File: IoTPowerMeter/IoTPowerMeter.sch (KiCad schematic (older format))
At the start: 50 parts, among them J1 Conn_01x01, J2 Conn_01x01, SW1 SW_SPDT, T1 VPP16-310, U1 UA78M33CDCYR, U2 ATM90E26-YU-B, U3 PHOTON, Y1 8.192MHz

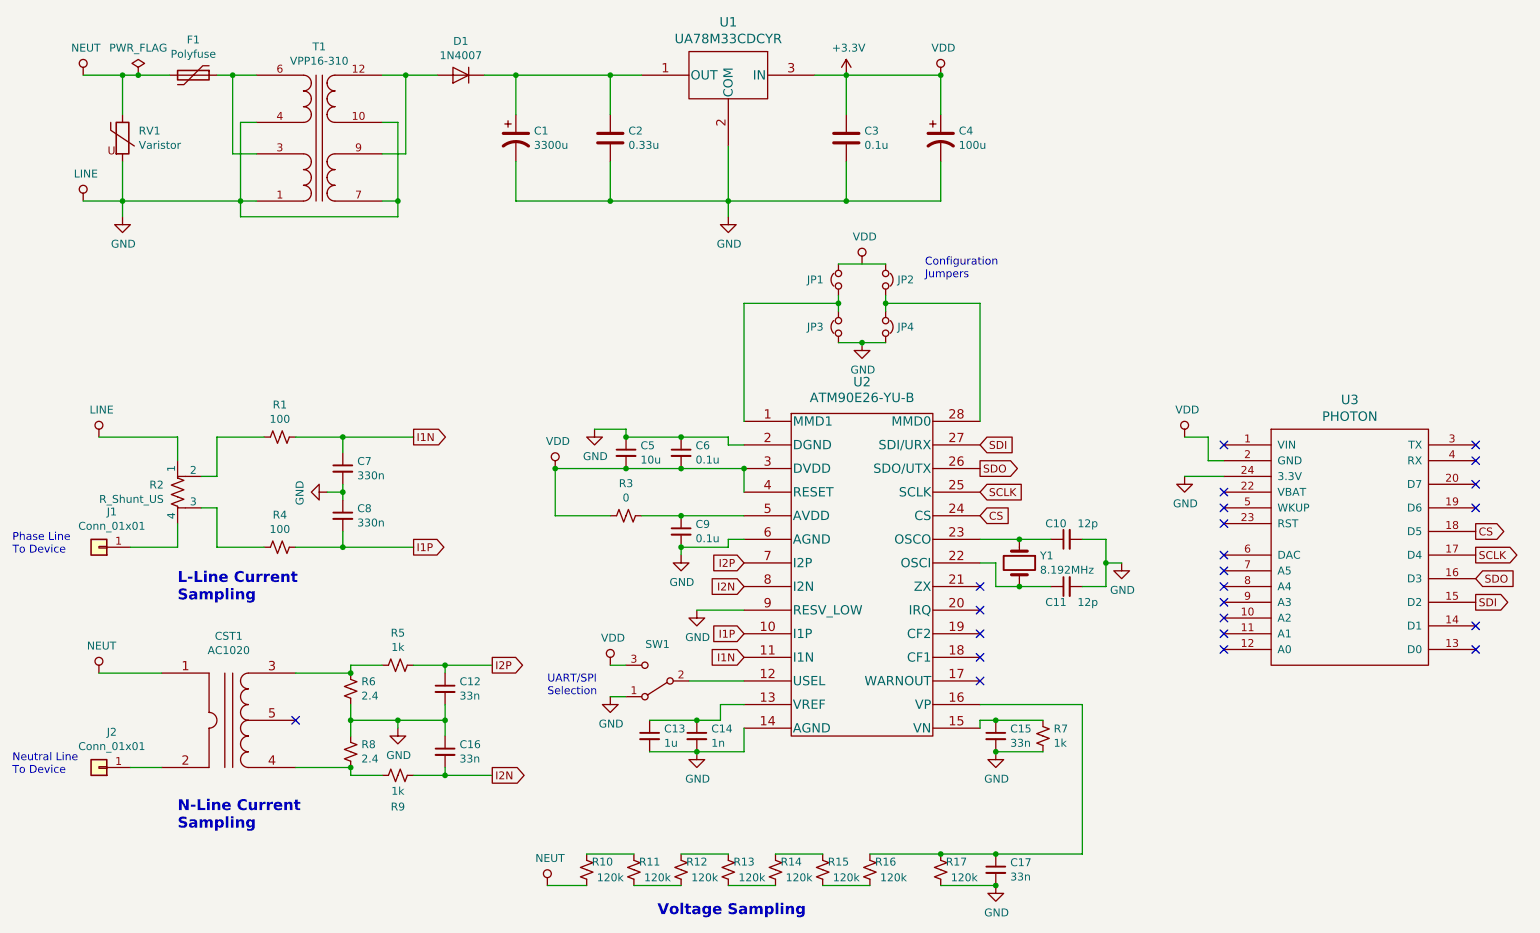
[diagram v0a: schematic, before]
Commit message: Updated incorrect values
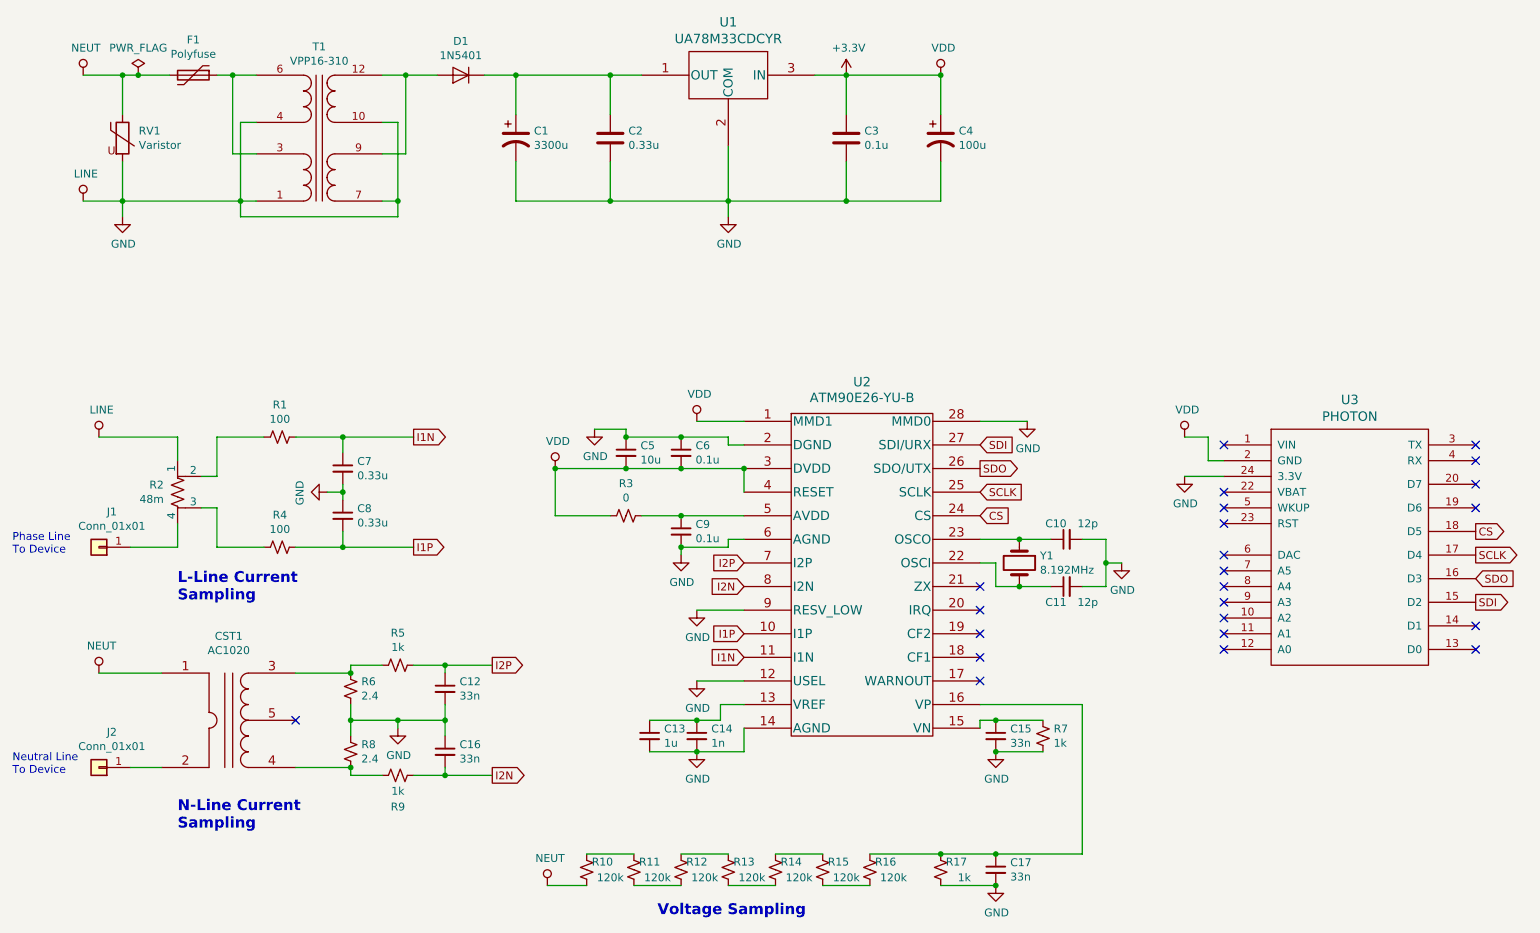
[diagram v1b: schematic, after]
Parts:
- removed JP1, JP2, JP3, JP4: Jumper_NC_Small, symbol Device:Jumper_NC_Small
- removed SW1: SW_SPDT, symbol Switch:SW_SPDT
- C7, C8: value 330n -> 0.33u
- D1: value 1N4007 -> 1N5401
- R17: value 120k -> 1k
- R2: value R_Shunt_US -> 48m
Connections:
- net +3V3: now also U2.1 (MMD1)
- net GND: now also U2.12 (USEL), U2.28 (MMD0)
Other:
- note removed: "Configuration \nJumpers"
- note removed: "UART/SPI\nSelection"
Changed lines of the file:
@@
 P 3500 1200
 F 0 "D1" H 3500 984 50  0000 C CNN
-F 1 "1N4007" H 3500 1075 50  0000 C CNN
+F 1 "1N5401" H 3500 1075 50  0000 C CNN
 F 2 "Diode_THT:D_DO-41_SOD81_P10.16mm_Horizontal" H 3500 1025 50  0001 C CNN
 F 3 "http://www.vishay.com/docs/88503/1n4001.pdf" H 3500 1200 50  0001 C CNN
@@
 P 1700 3850
 F 0 "R2" H 1612 3896 50  0000 R CNN
-F 1 "R_Shunt_US" H 1612 3805 50  0000 R CNN
+F 1 "48m" H 1612 3805 50  0000 R CNN
 F 2 "" V 1630 3850 50  0001 C CNN
 F 3 "~" H 1700 3850 50  0001 C CNN
@@
 P 2750 3700
 F 0 "C7" H 2842 3746 50  0000 L CNN
-F 1 "330n" H 2842 3655 50  0000 L CNN
+F 1 "0.33u" H 2842 3655 50  0000 L CNN
 F 2 "" H 2750 3700 50  0001 C CNN
 F 3 "~" H 2750 3700 50  0001 C CNN
@@
 P 2750 4000
 F 0 "C8" H 2842 4046 50  0000 L CNN
-F 1 "330n" H 2842 3955 50  0000 L CNN
+F 1 "0.33u" H 2842 3955 50  0000 L CNN
 F 2 "" H 2750 4000 50  0001 C CNN
 F 3 "~" H 2750 4000 50  0001 C CNN
@@
 $EndComp
 $Comp
-L Device:Jumper_NC_Small JP2
-U 1 1 5EBE4B13
-P 6200 2500
-F 0 "JP2" V 6200 2575 50  0000 L CNN
-F 1 "Jumper_NC_Small" V 6245 2574 50  0001 L CNN
-F 2 "" H 6200 2500 50  0001 C CNN
-F 3 "~" H 6200 2500 50  0001 C CNN
-	1    6200 2500
-	0    1    1    0
-$EndComp
-$Comp
-L Device:Jumper_NC_Small JP4
-U 1 1 5EBE6143
-P 6200 2800
-F 0 "JP4" V 6200 2875 50  0000 L CNN
-F 1 "Jumper_NC_Small" V 6245 2874 50  0001 L CNN
-F 2 "" H 6200 2800 50  0001 C CNN
-F 3 "~" H 6200 2800 50  0001 C CNN
-	1    6200 2800
-	0    1    1    0
-$EndComp
-$Comp
-L Device:Jumper_NC_Small JP3
-U 1 1 5EBE8CFF
-P 5900 2800
-F 0 "JP3" V 5900 3000 50  0000 R CNN
-F 1 "Jumper_NC_Small" V 5945 2874 50  0001 L CNN
-F 2 "" H 5900 2800 50  0001 C CNN
-F 3 "~" H 5900 2800 50  0001 C CNN
-	1    5900 2800
-	0    -1   -1   0
-$EndComp
-$Comp
-L Device:Jumper_NC_Small JP1
-U 1 1 5EBE8D05
-P 5900 2500
-F 0 "JP1" V 5900 2700 50  0000 R CNN
-F 1 "Jumper_NC_Small" V 5945 2574 50  0001 L CNN
-F 2 "" H 5900 2500 50  0001 C CNN
-F 3 "~" H 5900 2500 50  0001 C CNN
-	1    5900 2500
-	0    -1   -1   0
-$EndComp
-Wire Wire Line
-	5900 2600 5900 2650
-Wire Wire Line
-	6200 2600 6200 2650
-Wire Wire Line
-	6200 2400 5900 2400
-Wire Wire Line
-	5900 2900 6050 2900
-$Comp
 L power:GND #PWR08
 U 1 1 5EBF8404
-P 6050 2900
-F 0 "#PWR08" H 6050 2650 50  0001 C CNN
-F 1 "GND" H 6055 2727 50  0000 C CNN
-F 2 "" H 6050 2900 50  0001 C CNN
-F 3 "" H 6050 2900 50  0001 C CNN
-	1    6050 2900
-	1    0    0    -1
-$EndComp
-Connection ~ 6050 2900
-Wire Wire Line
-	6050 2900 6200 2900
+P 7100 3400
+F 0 "#PWR08" H 7100 3150 50  0001 C CNN
+F 1 "GND" H 7105 3227 50  0000 C CNN
+F 2 "" H 7100 3400 50  0001 C CNN
+F 3 "" H 7100 3400 50  0001 C CNN
+	1    7100 3400
+	1    0    0    -1
+$EndComp
 $Comp
 L power:VDD #PWR07
 U 1 1 5EBFCFF5
-P 6050 2400
-F 0 "#PWR07" H 6050 2250 50  0001 C CNN
-F 1 "VDD" H 6067 2573 50  0000 C CNN
-F 2 "" H 6050 2400 50  0001 C CNN
-F 3 "" H 6050 2400 50  0001 C CNN
-	1    6050 2400
-	1    0    0    -1
-$EndComp
-Wire Wire Line
-	5900 2650 5300 2650
-Wire Wire Line
-	5300 2650 5300 3400
-Connection ~ 5900 2650
-Wire Wire Line
-	5900 2650 5900 2700
-Wire Wire Line
-	6200 2650 6800 2650
-Wire Wire Line
-	6800 2650 6800 3400
-Connection ~ 6200 2650
-Wire Wire Line
-	6200 2650 6200 2700
-Text Notes 6450 2500 0    50   ~ 0
-Configuration \nJumpers
+P 5000 3400
+F 0 "#PWR07" H 5000 3250 50  0001 C CNN
+F 1 "VDD" H 5017 3573 50  0000 C CNN
+F 2 "" H 5000 3400 50  0001 C CNN
+F 3 "" H 5000 3400 50  0001 C CNN
+	1    5000 3400
+	1    0    0    -1
+$EndComp
 $Comp
 L Device:C_Small C5
@@
 $EndComp
 $Comp
-L Switch:SW_SPDT SW1
-U 1 1 5EC61A7F
-P 4750 5050
-F 0 "SW1" H 4750 4817 50  0000 C CNN
-F 1 "SW_SPDT" H 4750 4816 50  0001 C CNN
-F 2 "" H 4750 5050 50  0001 C CNN
-F 3 "~" H 4750 5050 50  0001 C CNN
-	1    4750 5050
-	-1   0    0    1
-$EndComp
-$Comp
-L power:VDD #PWR018
-U 1 1 5EC629FE
-P 4450 4950
-F 0 "#PWR018" H 4450 4800 50  0001 C CNN
-F 1 "VDD" H 4467 5123 50  0000 C CNN
-F 2 "" H 4450 4950 50  0001 C CNN
-F 3 "" H 4450 4950 50  0001 C CNN
-	1    4450 4950
-	1    0    0    -1
-$EndComp
-$Comp
 L power:GND #PWR020
 U 1 1 5EC65EEC
-P 4450 5150
-F 0 "#PWR020" H 4450 4900 50  0001 C CNN
-F 1 "GND" H 4455 4977 50  0000 C CNN
-F 2 "" H 4450 5150 50  0001 C CNN
-F 3 "" H 4450 5150 50  0001 C CNN
-	1    4450 5150
-	1    0    0    -1
-$EndComp
-Wire Wire Line
-	4550 4950 4450 4950
-Wire Wire Line
-	4550 5150 4450 5150
-Wire Wire Line
-	4950 5050 5300 5050
-Text Notes 4050 5150 0    50   ~ 0
-UART/SPI\nSelection
+P 5000 5050
+F 0 "#PWR020" H 5000 4800 50  0001 C CNN
+F 1 "GND" H 5005 4877 50  0000 C CNN
+F 2 "" H 5000 5050 50  0001 C CNN
+F 3 "" H 5000 5050 50  0001 C CNN
+	1    5000 5050
+	1    0    0    -1
+$EndComp
 $Comp
 L Device:C_Small C14
@@
 P 6550 6250
 F 0 "R17" H 6650 6300 50  0000 C CNN
-F 1 "120k" H 6700 6200 50  0000 C CNN
+F 1 "1k" H 6700 6200 50  0000 C CNN
 F 2 "" H 6550 6250 50  0001 C CNN
 F 3 "~" H 6550 6250 50  0001 C CNN
@@
 Text GLabel 9950 4100 2    50   Output ~ 0
 CS
+Wire Wire Line
+	5000 5050 5300 5050
+Wire Wire Line
+	5300 3400 5000 3400
+Wire Wire Line
+	6800 3400 7100 3400
 $EndSCHEMATC
